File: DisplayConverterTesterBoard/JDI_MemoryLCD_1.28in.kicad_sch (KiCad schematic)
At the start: 4 parts

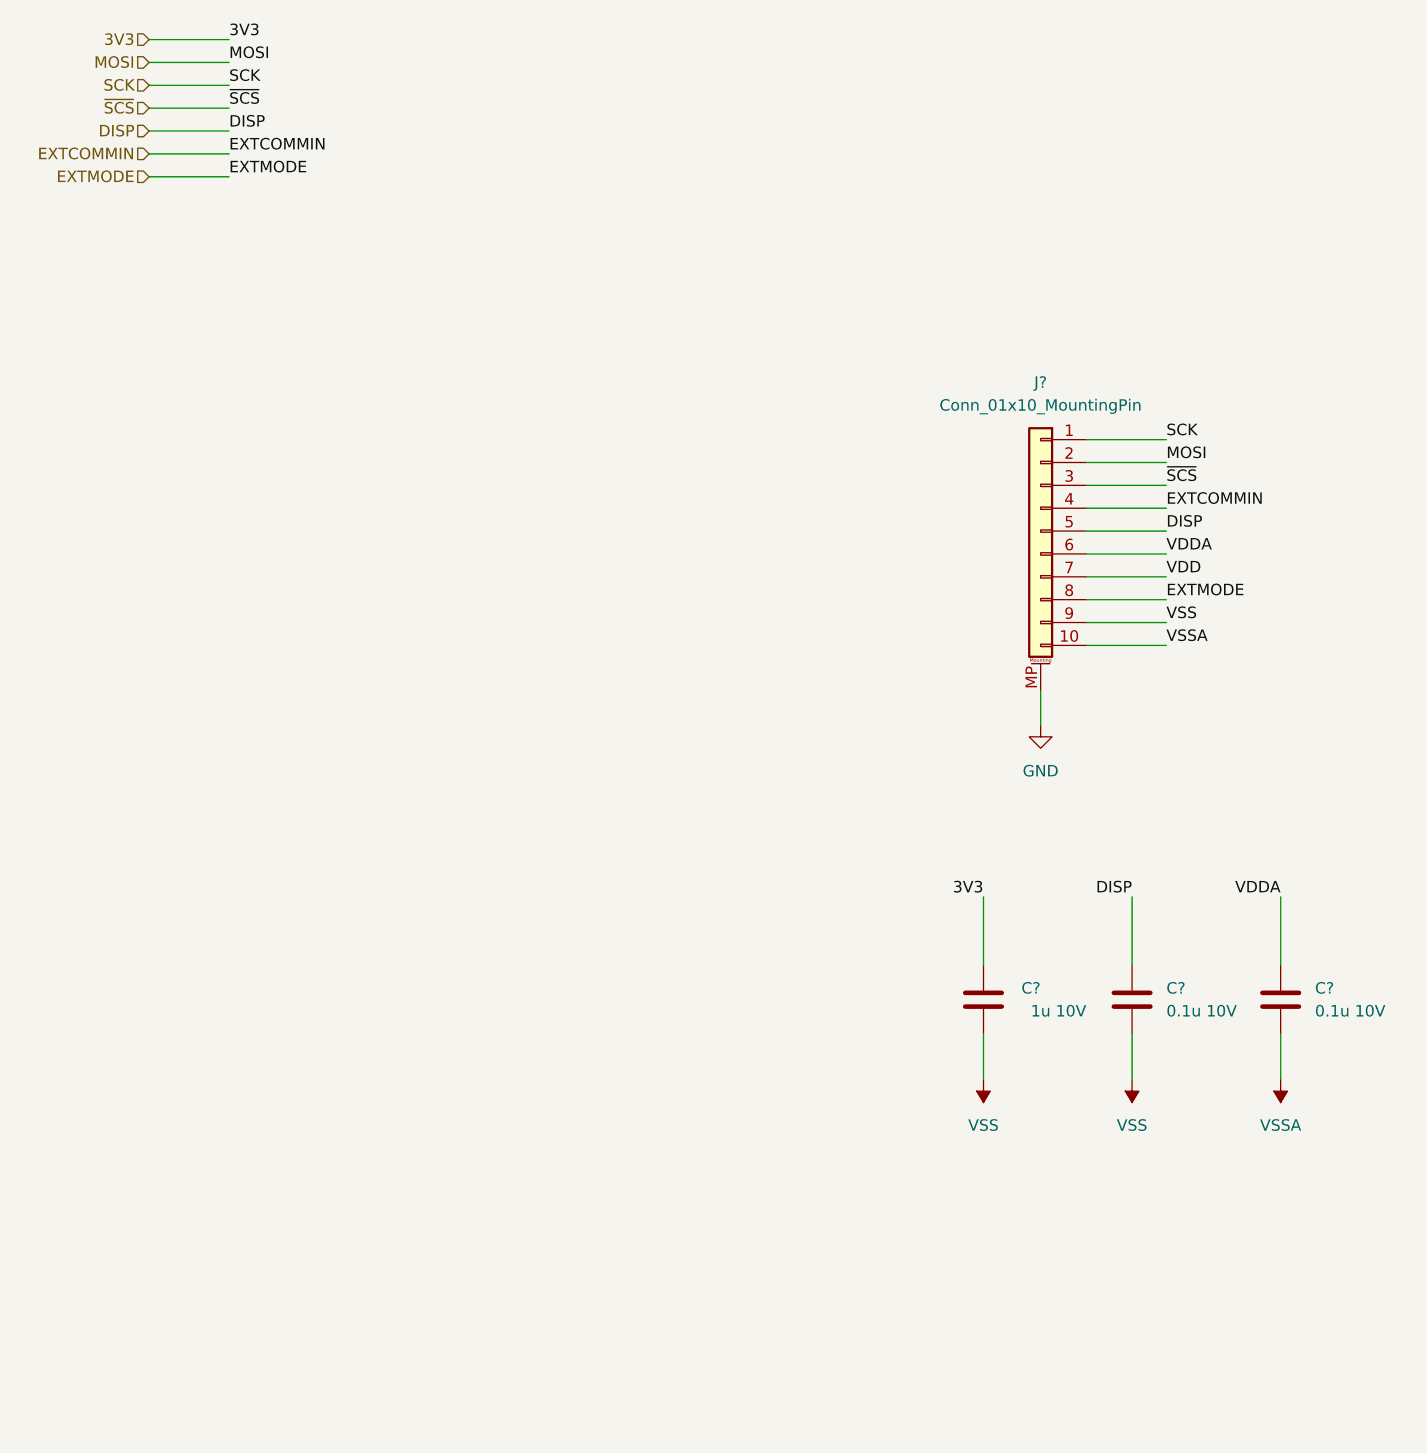
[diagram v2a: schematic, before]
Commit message: added jumper for extmode
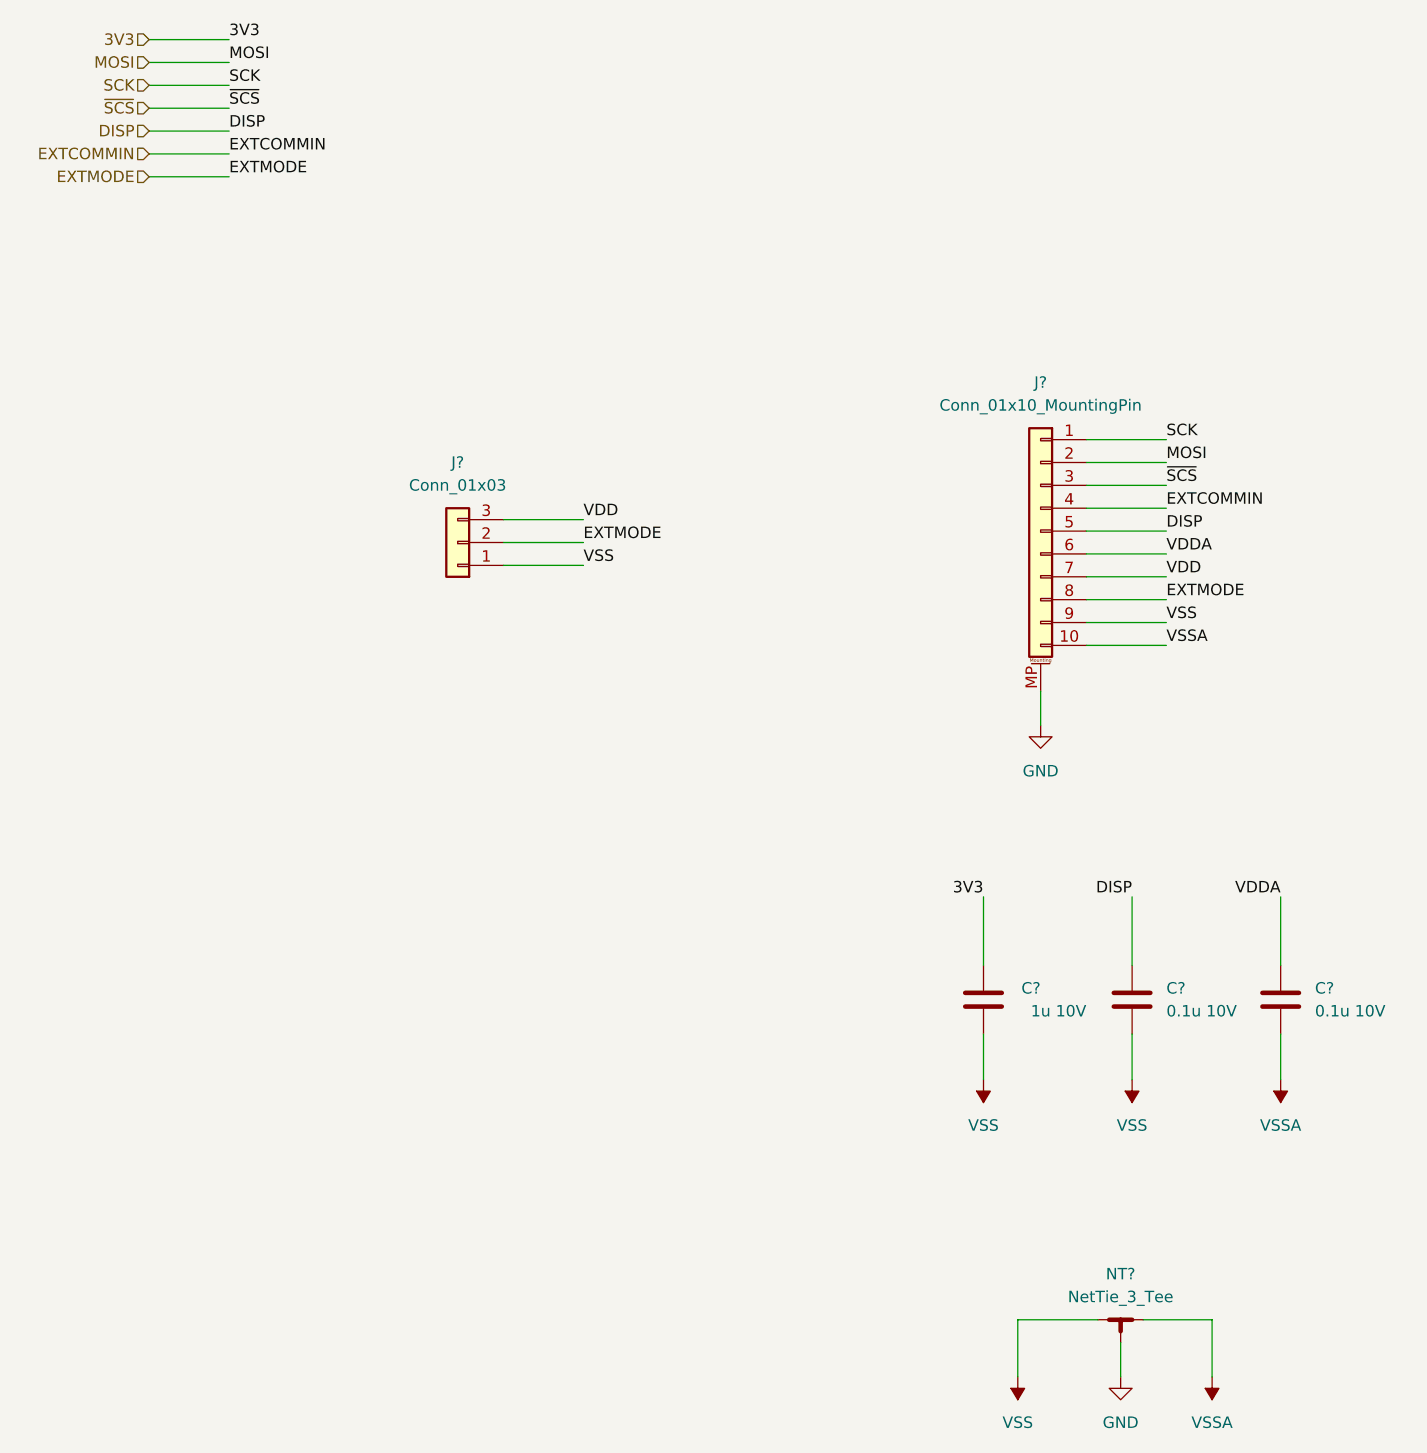
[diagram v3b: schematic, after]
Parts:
- added J?: Conn_01x03, Connector_PinHeader_2.54mm:PinHeader_1x03_P2.54mm_Vertical, symbol Connector_Generic:Conn_01x03
- added NT?: NetTie_3_Tee, symbol Device:NetTie_3_Tee
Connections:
- net EXTMODE: now also J?.2 (Pin_2)
- net GND: now also NT?.3
- net VDD: now also J?.3 (Pin_3)
- net VSS: now also J?.1 (Pin_1), NT?.1
- net VSSA: now also NT?.2
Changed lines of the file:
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@@
 (kicad_sch (version 20230121) (generator eeschema)
   (paper "A4")
+  (wire (pts (xy 72.39 83.82) (xy 81.28 83.82))
+    (stroke (width 0) (type default))
+  )
+  (wire (pts (xy 140.97 172.72) (xy 140.97 176.53))
+    (stroke (width 0) (type default))
+  )
   (wire (pts (xy 33.02 35.56) (xy 41.91 35.56))
     (stroke (width 0) (type default))
@@
     (stroke (width 0) (type default))
   )
+  (wire (pts (xy 72.39 81.28) (xy 81.28 81.28))
+    (stroke (width 0) (type default))
+  )
   (wire (pts (xy 158.75 123.19) (xy 158.75 130.81))
     (stroke (width 0) (type default))
@@
     (stroke (width 0) (type default))
   )
+  (wire (pts (xy 151.13 170.18) (xy 151.13 176.53))
+    (stroke (width 0) (type default))
+  )
   (wire (pts (xy 33.02 30.48) (xy 41.91 30.48))
     (stroke (width 0) (type default))
@@
     (stroke (width 0) (type default))
   )
+  (wire (pts (xy 143.51 170.18) (xy 151.13 170.18))
+    (stroke (width 0) (type default))
+  )
+  (wire (pts (xy 129.54 170.18) (xy 138.43 170.18))
+    (stroke (width 0) (type default))
+  )
+  (wire (pts (xy 72.39 86.36) (xy 81.28 86.36))
+    (stroke (width 0) (type default))
+  )
   (wire (pts (xy 142.24 138.43) (xy 142.24 143.51))
     (stroke (width 0) (type default))
@@
     (stroke (width 0) (type default))
   )
+  (wire (pts (xy 129.54 176.53) (xy 129.54 170.18))
+    (stroke (width 0) (type default))
+  )
   (wire (pts (xy 137.16 77.47) (xy 146.05 77.47))
     (stroke (width 0) (type default))
   )
+  (label "EXTMODE" (at 81.28 83.82 0) (fields_autoplaced)
+    (effects (font (size 1.27 1.27)) (justify left bottom))
+  )
   (label "~{SCS}" (at 41.91 35.56 0) (fields_autoplaced)
     (effects (font (size 1.27 1.27)) (justify left bottom))
@@
     (effects (font (size 1.27 1.27)) (justify left bottom))
   )
+  (label "VDD" (at 81.28 81.28 0) (fields_autoplaced)
+    (effects (font (size 1.27 1.27)) (justify left bottom))
+  )
   (label "EXTCOMMIN" (at 41.91 40.64 0) (fields_autoplaced)
     (effects (font (size 1.27 1.27)) (justify left bottom))
@@
   )
   (label "EXTMODE" (at 41.91 43.18 0) (fields_autoplaced)
+    (effects (font (size 1.27 1.27)) (justify left bottom))
+  )
+  (label "VSS" (at 81.28 86.36 0) (fields_autoplaced)
     (effects (font (size 1.27 1.27)) (justify left bottom))
   )
@@
     )
   )
+  (symbol (lib_id "Device:NetTie_3_Tee") (at 140.97 170.18 0) (unit 1)
+    (in_bom no) (on_board yes) (dnp no) (fields_autoplaced)
+    (property "Reference" "NT?" (at 140.97 165.1 0)
+      (effects (font (size 1.27 1.27)))
+    )
+    (property "Value" "NetTie_3_Tee" (at 140.97 167.64 0)
+      (effects (font (size 1.27 1.27)))
+    )
+    (property "Footprint" "" (at 140.97 170.18 0)
+      (effects (font (size 1.27 1.27)) hide)
+    )
+    (property "Datasheet" "~" (at 140.97 170.18 0)
+      (effects (font (size 1.27 1.27)) hide)
+    )
+    (pin "1")
+    (pin "2")
+    (pin "3")
+    (instances
+      (project "DisplayConverterTesterBoard"
+        (path "/58d9d6aa-d5e3-4b7b-b546-d57c329de758/0cb4f2ca-84b3-4b7f-ac05-316b1c40137b"
+          (reference "NT?") (unit 1)
+        )
+      )
+    )
+  )
   (symbol (lib_id "power:VSS") (at 142.24 143.51 180) (unit 1)
     (in_bom yes) (on_board yes) (dnp no) (fields_autoplaced)
@@
     )
   )
-  (symbol (lib_id "power:GND") (at 132.08 104.14 0) (unit 1)
-    (in_bom yes) (on_board yes) (dnp no) (fields_autoplaced)
-    (property "Reference" "#PWR0303" (at 132.08 110.49 0)
-      (effects (font (size 1.27 1.27)) hide)
-    )
-    (property "Value" "GND" (at 132.08 109.22 0)
-      (effects (font (size 1.27 1.27)))
-    )
-    (property "Footprint" "" (at 132.08 104.14 0)
-      (effects (font (size 1.27 1.27)) hide)
-    )
-    (property "Datasheet" "" (at 132.08 104.14 0)
+  (symbol (lib_id "Connector_Generic:Conn_01x03") (at 67.31 83.82 180) (unit 1)
+    (in_bom yes) (on_board yes) (dnp no) (fields_autoplaced)
+    (property "Reference" "J?" (at 67.31 74.93 0)
+      (effects (font (size 1.27 1.27)))
+    )
+    (property "Value" "Conn_01x03" (at 67.31 77.47 0)
+      (effects (font (size 1.27 1.27)))
+    )
+    (property "Footprint" "Connector_PinHeader_2.54mm:PinHeader_1x03_P2.54mm_Vertical" (at 67.31 83.82 0)
+      (effects (font (size 1.27 1.27)) hide)
+    )
+    (property "Datasheet" "~" (at 67.31 83.82 0)
+      (effects (font (size 1.27 1.27)) hide)
+    )
+    (pin "1")
+    (pin "2")
+    (pin "3")
+    (instances
+      (project "DisplayConverterTesterBoard"
+        (path "/58d9d6aa-d5e3-4b7b-b546-d57c329de758/0cb4f2ca-84b3-4b7f-ac05-316b1c40137b"
+          (reference "J?") (unit 1)
+        )
+      )
+    )
+  )
+  (symbol (lib_id "power:GND") (at 140.97 176.53 0) (unit 1)
+    (in_bom yes) (on_board yes) (dnp no) (fields_autoplaced)
+    (property "Reference" "#PWR0303" (at 140.97 182.88 0)
+      (effects (font (size 1.27 1.27)) hide)
+    )
+    (property "Value" "GND" (at 140.97 181.61 0)
+      (effects (font (size 1.27 1.27)))
+    )
+    (property "Footprint" "" (at 140.97 176.53 0)
+      (effects (font (size 1.27 1.27)) hide)
+    )
+    (property "Datasheet" "" (at 140.97 176.53 0)
       (effects (font (size 1.27 1.27)) hide)
     )
@@
         )
         (path "/58d9d6aa-d5e3-4b7b-b546-d57c329de758/0cb4f2ca-84b3-4b7f-ac05-316b1c40137b"
+          (reference "#PWR0404") (unit 1)
+        )
+      )
+    )
+  )
+  (symbol (lib_id "power:VSSA") (at 151.13 176.53 180) (unit 1)
+    (in_bom yes) (on_board yes) (dnp no) (fields_autoplaced)
+    (property "Reference" "#PWR0406" (at 151.13 172.72 0)
+      (effects (font (size 1.27 1.27)) hide)
+    )
+    (property "Value" "VSSA" (at 151.13 181.61 0)
+      (effects (font (size 1.27 1.27)))
+    )
+    (property "Footprint" "" (at 151.13 176.53 0)
+      (effects (font (size 1.27 1.27)) hide)
+    )
+    (property "Datasheet" "" (at 151.13 176.53 0)
+      (effects (font (size 1.27 1.27)) hide)
+    )
+    (pin "1")
+    (instances
+      (project "DisplayConverterTesterBoard"
+        (path "/58d9d6aa-d5e3-4b7b-b546-d57c329de758/0cb4f2ca-84b3-4b7f-ac05-316b1c40137b"
+          (reference "#PWR0406") (unit 1)
+        )
+      )
+    )
+  )
+  (symbol (lib_id "power:GND") (at 132.08 104.14 0) (unit 1)
+    (in_bom yes) (on_board yes) (dnp no) (fields_autoplaced)
+    (property "Reference" "#PWR0303" (at 132.08 110.49 0)
+      (effects (font (size 1.27 1.27)) hide)
+    )
+    (property "Value" "GND" (at 132.08 109.22 0)
+      (effects (font (size 1.27 1.27)))
+    )
+    (property "Footprint" "" (at 132.08 104.14 0)
+      (effects (font (size 1.27 1.27)) hide)
+    )
+    (property "Datasheet" "" (at 132.08 104.14 0)
+      (effects (font (size 1.27 1.27)) hide)
+    )
+    (pin "1")
+    (instances
+      (project "DisplayConverterTesterBoard"
+        (path "/58d9d6aa-d5e3-4b7b-b546-d57c329de758/edcee65f-25a8-4aef-871d-10e28d870fa2"
+          (reference "#PWR0303") (unit 1)
+        )
+        (path "/58d9d6aa-d5e3-4b7b-b546-d57c329de758/0cb4f2ca-84b3-4b7f-ac05-316b1c40137b"
           (reference "#PWR0405") (unit 1)
         )
@@
         )
       )
+    )
+  )
+  (symbol (lib_id "power:VSS") (at 129.54 176.53 180) (unit 1)
+    (in_bom yes) (on_board yes) (dnp no) (fields_autoplaced)
+    (property "Reference" "#PWR0407" (at 129.54 172.72 0)
+      (effects (font (size 1.27 1.27)) hide)
+    )
+    (property "Value" "VSS" (at 129.54 181.61 0)
+      (effects (font (size 1.27 1.27)))
+    )
+    (property "Footprint" "" (at 129.54 176.53 0)
+      (effects (font (size 1.27 1.27)) hide)
+    )
+    (property "Datasheet" "" (at 129.54 176.53 0)
+      (effects (font (size 1.27 1.27)) hide)
+    )
+    (pin "1")
+    (instances
+      (project "DisplayConverterTesterBoard"
+        (path "/58d9d6aa-d5e3-4b7b-b546-d57c329de758/0cb4f2ca-84b3-4b7f-ac05-316b1c40137b"
+          (reference "#PWR0407") (unit 1)
+        )
+      )

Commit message: annotate all components
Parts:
- gave numbers to parts that had none: 3
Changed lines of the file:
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@@
         )
         (path "/58d9d6aa-d5e3-4b7b-b546-d57c329de758/0cb4f2ca-84b3-4b7f-ac05-316b1c40137b"
-          (reference "C?") (unit 1)
+          (reference "C11") (unit 1)
         )
       )
@@
   (symbol (lib_id "Device:NetTie_3_Tee") (at 140.97 170.18 0) (unit 1)
     (in_bom no) (on_board yes) (dnp no) (fields_autoplaced)
-    (property "Reference" "NT?" (at 140.97 165.1 0)
+    (property "Reference" "NT2" (at 140.97 165.1 0)
       (effects (font (size 1.27 1.27)))
     )
@@
       (project "DisplayConverterTesterBoard"
         (path "/58d9d6aa-d5e3-4b7b-b546-d57c329de758/0cb4f2ca-84b3-4b7f-ac05-316b1c40137b"
-          (reference "NT?") (unit 1)
+          (reference "NT2") (unit 1)
         )
       )
@@
   (symbol (lib_id "Connector_Generic:Conn_01x03") (at 67.31 83.82 180) (unit 1)
     (in_bom yes) (on_board yes) (dnp no) (fields_autoplaced)
-    (property "Reference" "J?" (at 67.31 74.93 0)
+    (property "Reference" "J6" (at 67.31 74.93 0)
       (effects (font (size 1.27 1.27)))
     )
@@
       (project "DisplayConverterTesterBoard"
         (path "/58d9d6aa-d5e3-4b7b-b546-d57c329de758/0cb4f2ca-84b3-4b7f-ac05-316b1c40137b"
-          (reference "J?") (unit 1)
+          (reference "J6") (unit 1)
         )
       )
@@
         )
         (path "/58d9d6aa-d5e3-4b7b-b546-d57c329de758/0cb4f2ca-84b3-4b7f-ac05-316b1c40137b"
-          (reference "C?") (unit 1)
+          (reference "C12") (unit 1)
         )
       )
@@
   (symbol (lib_id "Connector_Generic_MountingPin:Conn_01x10_MountingPin") (at 132.08 82.55 0) (mirror y) (unit 1)
     (in_bom yes) (on_board yes) (dnp no) (fields_autoplaced)
-    (property "Reference" "J?" (at 132.08 66.04 0)
+    (property "Reference" "J7" (at 132.08 66.04 0)
       (effects (font (size 1.27 1.27)))
     )
@@
       (project "DisplayConverterTesterBoard"
         (path "/58d9d6aa-d5e3-4b7b-b546-d57c329de758/0cb4f2ca-84b3-4b7f-ac05-316b1c40137b"
-          (reference "J?") (unit 1)
+          (reference "J7") (unit 1)
         )
       )
@@
         )
         (path "/58d9d6aa-d5e3-4b7b-b546-d57c329de758/0cb4f2ca-84b3-4b7f-ac05-316b1c40137b"
-          (reference "C?") (unit 1)
-        )
-      )
+          (reference "C10") (unit 1)
+        )
+      )
